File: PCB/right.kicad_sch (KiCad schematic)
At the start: 46 parts

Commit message: update footpint
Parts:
- D22, D23, D24, D25, D26, D27, D28, D29, D30, D31, D32, D33, D34, D35, D36, D37, D38, D39, D40, D41, D42: footprint kometa:Diode -> kometa:D_SOD323
- PS_R1: footprint kometa:MSK-12C02 -> kometa:SW_MSK-12C02
- PW_R1: footprint kometa:Battery -> kometa:J_Battery
- R_R1: footprint kometa:Reset -> kometa:SW_TS342A2P
- SM_R1: footprint kometa:SuperMini -> kometa:U_ProMicro_nRF52840
- SW22, SW23, SW24, SW25, SW26, SW27, SW28, SW29, SW30, SW31, SW32, SW33, SW34, SW35, SW36, SW37, SW38, SW39, SW40, SW41, SW42: footprint kometa:ChocV2 -> kometa:SW_Hotswap_Kailh_Choc_V1V2
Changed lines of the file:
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@@
 			)
 		)
-		(property "Footprint" "kometa:ChocV2"
+		(property "Footprint" "kometa:SW_Hotswap_Kailh_Choc_V1V2"
 			(at 64.516 93.98 0)
 			(effects
@@
 			)
 		)
-		(property "Footprint" "kometa:ChocV2"
+		(property "Footprint" "kometa:SW_Hotswap_Kailh_Choc_V1V2"
 			(at 135.636 130.81 0)
 			(effects
@@
 			)
 		)
-		(property "Footprint" "kometa:Diode"
+		(property "Footprint" "kometa:D_SOD323"
 			(at 136.906 108.712 0)
 			(effects
@@
 			)
 		)
-		(property "Footprint" "kometa:Diode"
+		(property "Footprint" "kometa:D_SOD323"
 			(at 83.566 127.762 0)
 			(effects
@@
 			)
 		)
-		(property "Footprint" "kometa:ChocV2"
+		(property "Footprint" "kometa:SW_Hotswap_Kailh_Choc_V1V2"
 			(at 64.516 111.76 0)
 			(effects
@@
 			)
 		)
-		(property "Footprint" "kometa:Diode"
+		(property "Footprint" "kometa:D_SOD323"
 			(at 101.346 127.762 0)
 			(effects
@@
 			)
 		)
-		(property "Footprint" "kometa:ChocV2"
+		(property "Footprint" "kometa:SW_Hotswap_Kailh_Choc_V1V2"
 			(at 46.736 130.81 0)
 			(effects
@@
 			)
 		)
-		(property "Footprint" "kometa:ChocV2"
+		(property "Footprint" "kometa:SW_Hotswap_Kailh_Choc_V1V2"
 			(at 135.636 111.76 0)
 			(effects
@@
 			)
 		)
-		(property "Footprint" "kometa:Diode"
+		(property "Footprint" "kometa:D_SOD323"
 			(at 83.566 108.712 0)
 			(effects
@@
 			)
 		)
-		(property "Footprint" "kometa:ChocV2"
+		(property "Footprint" "kometa:SW_Hotswap_Kailh_Choc_V1V2"
 			(at 117.856 130.81 0)
 			(effects
@@
 			)
 		)
-		(property "Footprint" "kometa:Diode"
+		(property "Footprint" "kometa:D_SOD323"
 			(at 119.126 108.712 0)
 			(effects
@@
 			)
 		)
-		(property "Footprint" "kometa:Diode"
+		(property "Footprint" "kometa:D_SOD323"
 			(at 136.906 90.932 0)
 			(effects
@@
 			)
 		)
-		(property "Footprint" "kometa:Diode"
+		(property "Footprint" "kometa:D_SOD323"
 			(at 101.346 90.932 0)
 			(effects
@@
 			)
 		)
-		(property "Footprint" "kometa:Diode"
+		(property "Footprint" "kometa:D_SOD323"
 			(at 65.786 143.002 0)
 			(effects
@@
 			)
 		)
-		(property "Footprint" "kometa:ChocV2"
+		(property "Footprint" "kometa:SW_Hotswap_Kailh_Choc_V1V2"
 			(at 135.636 93.98 0)
 			(effects
@@
 			)
 		)
-		(property "Footprint" "kometa:Diode"
+		(property "Footprint" "kometa:D_SOD323"
 			(at 48.006 90.932 0)
 			(effects
@@
 			)
 		)
-		(property "Footprint" "kometa:ChocV2"
+		(property "Footprint" "kometa:SW_Hotswap_Kailh_Choc_V1V2"
 			(at 46.736 146.05 0)
 			(effects
@@
 			)
 		)
-		(property "Footprint" "kometa:Diode"
+		(property "Footprint" "kometa:D_SOD323"
 			(at 65.786 90.932 0)
 			(effects
@@
 			)
 		)
-		(property "Footprint" "kometa:Reset"
+		(property "Footprint" "kometa:SW_TS342A2P"
 			(at 176.53 119.38 0)
 			(effects
@@
 			)
 		)
-		(property "Footprint" "kometa:Battery"
+		(property "Footprint" "kometa:J_Battery"
 			(at 167.894 89.916 0)
 			(effects
@@
 			)
 		)
-		(property "Footprint" "kometa:Diode"
+		(property "Footprint" "kometa:D_SOD323"
 			(at 119.126 90.932 0)
 			(effects
@@
 			)
 		)
-		(property "Footprint" "kometa:Diode"
+		(property "Footprint" "kometa:D_SOD323"
 			(at 136.906 127.762 0)
 			(effects
@@
 			)
 		)
-		(property "Footprint" "kometa:ChocV2"
+		(property "Footprint" "kometa:SW_Hotswap_Kailh_Choc_V1V2"
 			(at 117.856 93.98 0)
 			(effects
@@
 			)
 		)
-		(property "Footprint" "kometa:Diode"
+		(property "Footprint" "kometa:D_SOD323"
 			(at 48.006 143.002 0)
 			(effects
@@
 			)
 		)
-		(property "Footprint" "kometa:ChocV2"
+		(property "Footprint" "kometa:SW_Hotswap_Kailh_Choc_V1V2"
 			(at 82.296 146.05 0)
 			(effects
@@
 			)
 		)
-		(property "Footprint" "kometa:Diode"
+		(property "Footprint" "kometa:D_SOD323"
 			(at 83.566 143.002 0)
 			(effects
@@
 			)
 		)
-		(property "Footprint" "kometa:ChocV2"
+		(property "Footprint" "kometa:SW_Hotswap_Kailh_Choc_V1V2"
 			(at 100.076 111.76 0)
 			(effects
@@
 			)
 		)
-		(property "Footprint" "kometa:ChocV2"
+		(property "Footprint" "kometa:SW_Hotswap_Kailh_Choc_V1V2"
 			(at 100.076 130.81 0)
 			(effects
@@
 			)
 		)
-		(property "Footprint" "kometa:ChocV2"
+		(property "Footprint" "kometa:SW_Hotswap_Kailh_Choc_V1V2"
 			(at 64.516 146.05 0)
 			(effects
@@
 			)
 		)
-		(property "Footprint" "kometa:ChocV2"
+		(property "Footprint" "kometa:SW_Hotswap_Kailh_Choc_V1V2"
 			(at 46.736 93.98 0)
 			(effects
@@
 			)
 		)
-		(property "Footprint" "kometa:Diode"
+		(property "Footprint" "kometa:D_SOD323"
 			(at 65.786 108.712 0)
 			(effects
@@
 			)
 		)
-		(property "Footprint" "kometa:ChocV2"
+		(property "Footprint" "kometa:SW_Hotswap_Kailh_Choc_V1V2"
 			(at 82.296 111.76 0)
 			(effects
@@
 			)
 		)
-		(property "Footprint" "kometa:ChocV2"
+		(property "Footprint" "kometa:SW_Hotswap_Kailh_Choc_V1V2"
 			(at 46.736 111.76 0)
 			(effects
@@
 			)
 		)
-		(property "Footprint" "kometa:Diode"
+		(property "Footprint" "kometa:D_SOD323"
 			(at 48.006 108.712 0)
 			(effects
@@
 			)
 		)
-		(property "Footprint" "kometa:ChocV2"
+		(property "Footprint" "kometa:SW_Hotswap_Kailh_Choc_V1V2"
 			(at 117.856 111.76 0)
 			(effects
@@
 			)
 		)
-		(property "Footprint" "kometa:Diode"
+		(property "Footprint" "kometa:D_SOD323"
 			(at 48.006 127.762 0)
 			(effects
@@
 			)
 		)
-		(property "Footprint" "kometa:ChocV2"
+		(property "Footprint" "kometa:SW_Hotswap_Kailh_Choc_V1V2"
 			(at 64.516 130.81 0)
 			(effects
@@
 			)
 		)
-		(property "Footprint" "kometa:Diode"
+		(property "Footprint" "kometa:D_SOD323"
 			(at 119.126 127.762 0)
 			(effects
@@
 			)
 		)
-		(property "Footprint" "kometa:SuperMini"
+		(property "Footprint" "kometa:U_ProMicro_nRF52840"
 			(at 233.68 119.888 0)
 			(effects
@@
 			)
 		)
-		(property "Footprint" "kometa:ChocV2"
+		(property "Footprint" "kometa:SW_Hotswap_Kailh_Choc_V1V2"
 			(at 82.296 93.98 0)
 			(effects
@@
 			)
 		)
-		(property "Footprint" "kometa:ChocV2"
+		(property "Footprint" "kometa:SW_Hotswap_Kailh_Choc_V1V2"
 			(at 82.296 130.81 0)
 			(effects
@@
 			)
 		)
-		(property "Footprint" "kometa:MSK-12C02"
+		(property "Footprint" "kometa:SW_MSK-12C02"
 			(at 178.054 91.694 0)
 			(effects
@@
 			)
 		)
-		(property "Footprint" "kometa:Diode"
+		(property "Footprint" "kometa:D_SOD323"
 			(at 101.346 108.712 0)
 			(effects
@@
 			)
 		)
-		(property "Footprint" "kometa:Diode"
+		(property "Footprint" "kometa:D_SOD323"
 			(at 83.566 90.932 0)
 			(effects
@@
 			)
 		)
-		(property "Footprint" "kometa:ChocV2"
+		(property "Footprint" "kometa:SW_Hotswap_Kailh_Choc_V1V2"
 			(at 100.076 93.98 0)
 			(effects
@@
 			)
 		)
-		(property "Footprint" "kometa:Diode"
+		(property "Footprint" "kometa:D_SOD323"
 			(at 65.786 127.762 0)
 			(effects

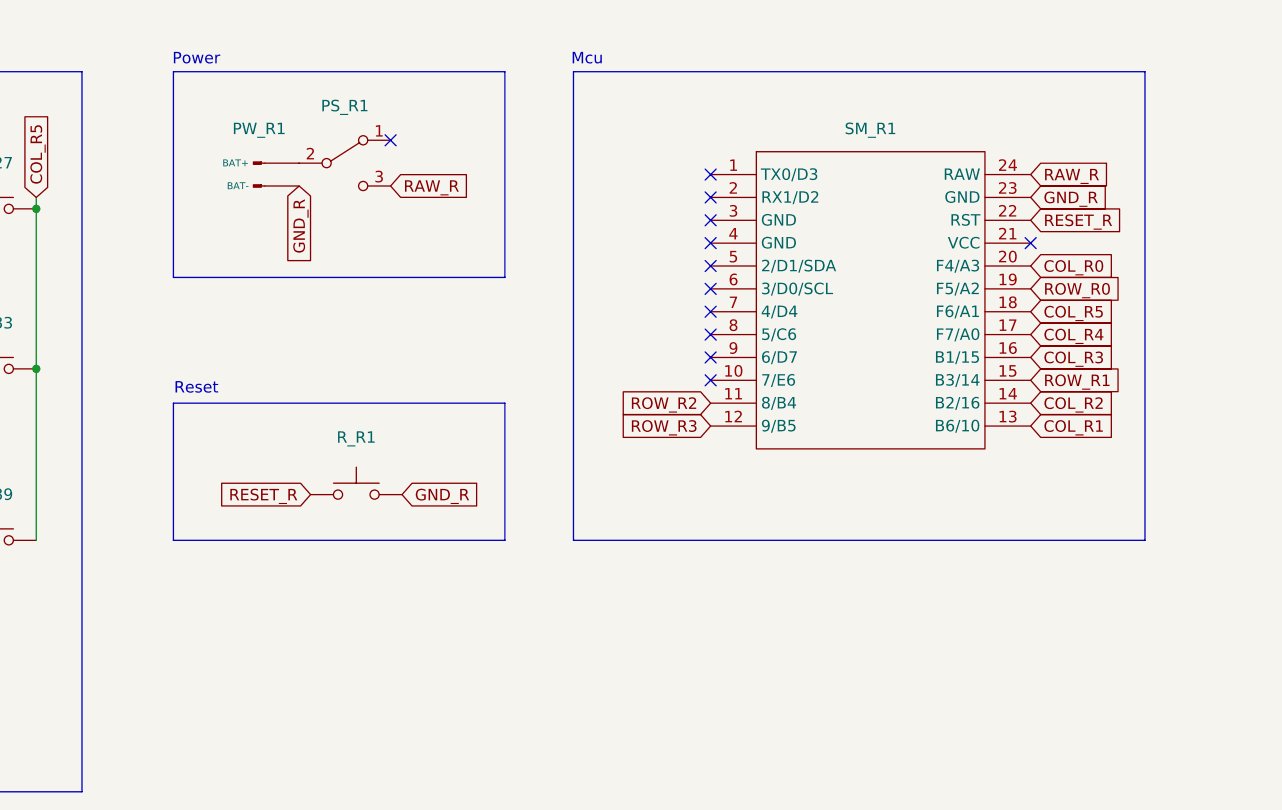
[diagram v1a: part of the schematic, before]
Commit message: add led sh and pretty
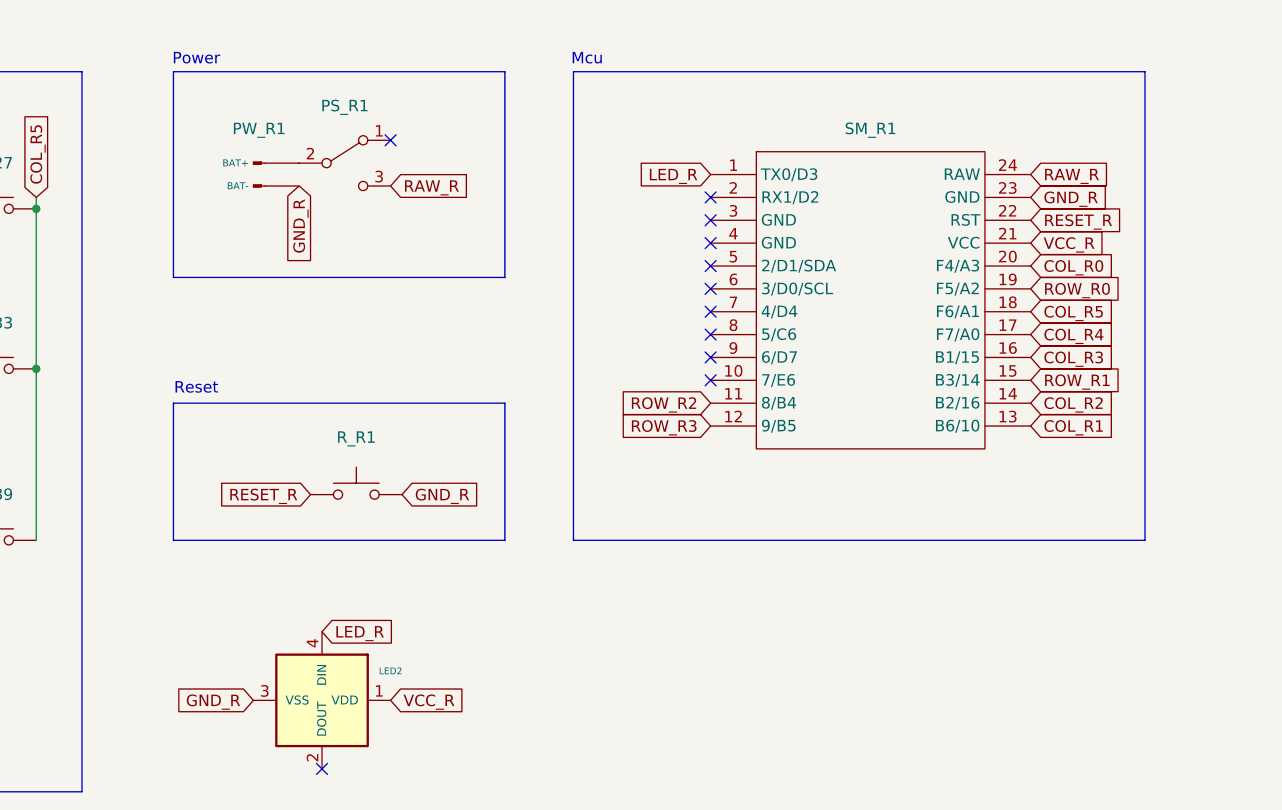
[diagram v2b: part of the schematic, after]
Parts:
- added LED2: ~, kometa:YS-SK6812MINI-E, symbol kometa:YS-SK6812MINI-E
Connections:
- net GND_R: now also LED2.3 (VSS)
- net LED_R: now reaches SM_R1.1 (TX0/D3)
- net LED_R: now also LED2.4 (DIN)
- net VCC_R: now reaches SM_R1.21 (VCC)
- net VCC_R: now also LED2.1 (VDD)
- no-connect marks 13 -> 12
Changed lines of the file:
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@@
 	)
 	(no_connect
-		(at 215.9 83.82)
-	)
-	(no_connect
 		(at 215.9 88.9)
 	)
@@
 	)
 	(no_connect
+		(at 172.72 149.86)
+	)
+	(no_connect
 		(at 215.9 99.06)
 	)
@@
 	)
 	(no_connect
-		(at 251.46 91.44)
-	)
-	(no_connect
 		(at 215.9 96.52)
 	)
@@
 		)
 	)
+	(global_label "LED_R"
+		(shape input)
+		(at 172.72 134.62 0)
+		(fields_autoplaced yes)
+		(effects
+			(font
+				(size 1.27 1.27)
+			)
+			(justify left)
+		)
+		(property "Intersheetrefs" "${INTERSHEET_REFS}"
+			(at 181.3899 134.62 0)
+			(effects
+				(font
+					(size 1.27 1.27)
+				)
+				(justify left)
+				(hide yes)
+			)
+		)
+	)
 	(global_label "ROW_R1"
 		(shape input)
@@
 		)
 	)
+	(global_label "GND_R"
+		(shape input)
+		(at 165.1 142.24 180)
+		(fields_autoplaced yes)
+		(effects
+			(font
+				(size 1.27 1.27)
+			)
+			(justify right)
+		)
+		(property "Intersheetrefs" "${INTERSHEET_REFS}"
+			(at 156.0067 142.24 0)
+			(effects
+				(font
+					(size 1.27 1.27)
+				)
+				(justify right)
+				(hide yes)
+			)
+		)
+	)
 	(global_label "COL_R5"
 		(shape input)
@@
 		)
 	)
+	(global_label "VCC_R"
+		(shape input)
+		(at 251.46 91.44 0)
+		(fields_autoplaced yes)
+		(effects
+			(font
+				(size 1.27 1.27)
+			)
+			(justify left)
+		)
+		(property "Intersheetrefs" "${INTERSHEET_REFS}"
+			(at 260.3114 91.44 0)
+			(effects
+				(font
+					(size 1.27 1.27)
+				)
+				(justify left)
+				(hide yes)
+			)
+		)
+	)
+	(global_label "LED_R"
+		(shape input)
+		(at 215.9 83.82 180)
+		(fields_autoplaced yes)
+		(effects
+			(font
+				(size 1.27 1.27)
+			)
+			(justify right)
+		)
+		(property "Intersheetrefs" "${INTERSHEET_REFS}"
+			(at 207.2301 83.82 0)
+			(effects
+				(font
+					(size 1.27 1.27)
+				)
+				(justify right)
+				(hide yes)
+			)
+		)
+	)
 	(global_label "COL_R1"
 		(shape input)
@@
 		)
 	)
+	(global_label "VCC_R"
+		(shape input)
+		(at 180.34 142.24 0)
+		(fields_autoplaced yes)
+		(effects
+			(font
+				(size 1.27 1.27)
+			)
+			(justify left)
+		)
+		(property "Intersheetrefs" "${INTERSHEET_REFS}"
+			(at 189.1914 142.24 0)
+			(effects
+				(font
+					(size 1.27 1.27)
+				)
+				(justify left)
+				(hide yes)
+			)
+		)
+	)
 	(symbol
 		(lib_id "kometa:Keyswitch")
@@
 					(unit 1)
 				)
+			)
+		)
+	)
+	(symbol
+		(lib_id "kometa:YS-SK6812MINI-E")
+		(at 172.72 142.24 0)
+		(unit 1)
+		(exclude_from_sim no)
+		(in_bom yes)
+		(on_board yes)
+		(dnp no)
+		(fields_autoplaced yes)
+		(property "Reference" "LED2"
+			(at 180.34 138.9949 0)
+			(effects
+				(font
+					(size 0.7366 0.7366)
+				)
+			)
+		)
+		(property "Value" "~"
+			(at 179.324 148.59 0)
+			(effects
+				(font
+					(size 0.7366 0.7366)
+				)
+				(hide yes)
+			)
+		)
+		(property "Footprint" "kometa:YS-SK6812MINI-E"
+			(at 175.26 148.59 0)
+			(effects
+				(font
+					(size 1.27 1.27)
+				)
+				(hide yes)
+			)
+		)
+		(property "Datasheet" ""
+			(at 175.26 148.59 0)
+			(effects
+				(font
+					(size 1.27 1.27)
+				)
+				(hide yes)
+			)
+		)
+		(property "Description" ""
+			(at 172.72 142.24 0)
+			(effects
+				(font
+					(size 1.27 1.27)
+				)
+				(hide yes)
+			)
+		)
+		(pin "3"
+		)
+		(pin "4"
+		)
+		(pin "1"
+		)
+		(pin "2"
+		)
+		(instances
+			(project "KOMETA"
+				(path "/87d0d44c-3cdf-4c1b-91f4-ef0852a5e1e5/a35db046-83b9-48ee-bc16-fc20ad35d452"
+					(reference "LED2")
+					(unit 1)
+				)

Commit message: Experimental KS27/KS33 support
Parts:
- SW22, SW23, SW24, SW25, SW26, SW27, SW28, SW29, SW30, SW31, SW32, SW33, SW34, SW35, SW36, SW37, SW38, SW39, SW40, SW41, SW42: footprint kometa:SW_Hotswap_Kailh_Choc_V1V2 -> kometa:SW_Hotswap_Kailh_Choc_V1V2_with_KS27_KS33
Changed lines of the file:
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@@
 			)
 		)
-		(property "Footprint" "kometa:SW_Hotswap_Kailh_Choc_V1V2"
+		(property "Footprint" "kometa:SW_Hotswap_Kailh_Choc_V1V2_with_KS27_KS33"
 			(at 64.516 93.98 0)
 			(effects
@@
 			)
 		)
-		(property "Footprint" "kometa:SW_Hotswap_Kailh_Choc_V1V2"
+		(property "Footprint" "kometa:SW_Hotswap_Kailh_Choc_V1V2_with_KS27_KS33"
 			(at 135.636 130.81 0)
 			(effects
@@
 			)
 		)
-		(property "Footprint" "kometa:SW_Hotswap_Kailh_Choc_V1V2"
+		(property "Footprint" "kometa:SW_Hotswap_Kailh_Choc_V1V2_with_KS27_KS33"
 			(at 64.516 111.76 0)
 			(effects
@@
 			)
 		)
-		(property "Footprint" "kometa:SW_Hotswap_Kailh_Choc_V1V2"
+		(property "Footprint" "kometa:SW_Hotswap_Kailh_Choc_V1V2_with_KS27_KS33"
 			(at 46.736 130.81 0)
 			(effects
@@
 			)
 		)
-		(property "Footprint" "kometa:SW_Hotswap_Kailh_Choc_V1V2"
+		(property "Footprint" "kometa:SW_Hotswap_Kailh_Choc_V1V2_with_KS27_KS33"
 			(at 135.636 111.76 0)
 			(effects
@@
 			)
 		)
-		(property "Footprint" "kometa:SW_Hotswap_Kailh_Choc_V1V2"
+		(property "Footprint" "kometa:SW_Hotswap_Kailh_Choc_V1V2_with_KS27_KS33"
 			(at 117.856 130.81 0)
 			(effects
@@
 			)
 		)
-		(property "Footprint" "kometa:SW_Hotswap_Kailh_Choc_V1V2"
+		(property "Footprint" "kometa:SW_Hotswap_Kailh_Choc_V1V2_with_KS27_KS33"
 			(at 135.636 93.98 0)
 			(effects
@@
 			)
 		)
-		(property "Footprint" "kometa:SW_Hotswap_Kailh_Choc_V1V2"
+		(property "Footprint" "kometa:SW_Hotswap_Kailh_Choc_V1V2_with_KS27_KS33"
 			(at 46.736 146.05 0)
 			(effects
@@
 			)
 		)
-		(property "Footprint" "kometa:SW_Hotswap_Kailh_Choc_V1V2"
+		(property "Footprint" "kometa:SW_Hotswap_Kailh_Choc_V1V2_with_KS27_KS33"
 			(at 117.856 93.98 0)
 			(effects
@@
 			)
 		)
-		(property "Footprint" "kometa:SW_Hotswap_Kailh_Choc_V1V2"
+		(property "Footprint" "kometa:SW_Hotswap_Kailh_Choc_V1V2_with_KS27_KS33"
 			(at 82.296 146.05 0)
 			(effects
@@
 			)
 		)
-		(property "Footprint" "kometa:SW_Hotswap_Kailh_Choc_V1V2"
+		(property "Footprint" "kometa:SW_Hotswap_Kailh_Choc_V1V2_with_KS27_KS33"
 			(at 100.076 111.76 0)
 			(effects
@@
 			)
 		)
-		(property "Footprint" "kometa:SW_Hotswap_Kailh_Choc_V1V2"
+		(property "Footprint" "kometa:SW_Hotswap_Kailh_Choc_V1V2_with_KS27_KS33"
 			(at 100.076 130.81 0)
 			(effects
@@
 			)
 		)
-		(property "Footprint" "kometa:SW_Hotswap_Kailh_Choc_V1V2"
+		(property "Footprint" "kometa:SW_Hotswap_Kailh_Choc_V1V2_with_KS27_KS33"
 			(at 64.516 146.05 0)
 			(effects
@@
 			)
 		)
-		(property "Footprint" "kometa:SW_Hotswap_Kailh_Choc_V1V2"
+		(property "Footprint" "kometa:SW_Hotswap_Kailh_Choc_V1V2_with_KS27_KS33"
 			(at 46.736 93.98 0)
 			(effects
@@
 			)
 		)
-		(property "Footprint" "kometa:SW_Hotswap_Kailh_Choc_V1V2"
+		(property "Footprint" "kometa:SW_Hotswap_Kailh_Choc_V1V2_with_KS27_KS33"
 			(at 82.296 111.76 0)
 			(effects
@@
 			)
 		)
-		(property "Footprint" "kometa:SW_Hotswap_Kailh_Choc_V1V2"
+		(property "Footprint" "kometa:SW_Hotswap_Kailh_Choc_V1V2_with_KS27_KS33"
 			(at 46.736 111.76 0)
 			(effects
@@
 			)
 		)
-		(property "Footprint" "kometa:SW_Hotswap_Kailh_Choc_V1V2"
+		(property "Footprint" "kometa:SW_Hotswap_Kailh_Choc_V1V2_with_KS27_KS33"
 			(at 117.856 111.76 0)
 			(effects
@@
 			)
 		)
-		(property "Footprint" "kometa:SW_Hotswap_Kailh_Choc_V1V2"
+		(property "Footprint" "kometa:SW_Hotswap_Kailh_Choc_V1V2_with_KS27_KS33"
 			(at 64.516 130.81 0)
 			(effects
@@
 			)
 		)
-		(property "Footprint" "kometa:SW_Hotswap_Kailh_Choc_V1V2"
+		(property "Footprint" "kometa:SW_Hotswap_Kailh_Choc_V1V2_with_KS27_KS33"
 			(at 82.296 93.98 0)
 			(effects
@@
 			)
 		)
-		(property "Footprint" "kometa:SW_Hotswap_Kailh_Choc_V1V2"
+		(property "Footprint" "kometa:SW_Hotswap_Kailh_Choc_V1V2_with_KS27_KS33"
 			(at 82.296 130.81 0)
 			(effects
@@
 			)
 		)
-		(property "Footprint" "kometa:SW_Hotswap_Kailh_Choc_V1V2"
+		(property "Footprint" "kometa:SW_Hotswap_Kailh_Choc_V1V2_with_KS27_KS33"
 			(at 100.076 93.98 0)
 			(effects
